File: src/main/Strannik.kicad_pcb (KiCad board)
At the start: 2 copper layers, 139 x 129 mm, 104 parts, among them J1 Thumb cluster, J2 Battery, SW1 Reset, SW11 SW_Push_Dual, SW12 SW_Push_Dual, SW13 SW_Push_Dual, SW14 SW_Push_Dual, SW15 SW_Push_Dual, SW16 SW_Push_Dual, SW17 SW_Push_Dual, SW21 SW_Push_Dual, SW22 SW_Push_Dual, SW23 SW_Push_Dual, SW24 SW_Push_Dual, SW25 SW_Push_Dual, SW26 SW_Push_Dual, SW27 SW_Push_Dual, SW31 SW_Push_Dual, SW32 SW_Push_Dual, SW33 SW_Push_Dual, SW34 SW_Push_Dual, SW35 SW_Push_Dual, SW36 SW_Push_Dual, SW37 SW_Push_Dual, SW41 SW_Push_Dual, SW42 SW_Push_Dual, SW43 SW_Push_Dual, SW44 SW_Push_Dual, SW45 SW_Push_Dual, SW46 SW_Push_Dual, SW51 SW_Push_Dual, SW52 SW_Push_Dual, SW53 SW_Push_Dual, SW54 SW_Push_Dual, SW55 SW_Push_Dual

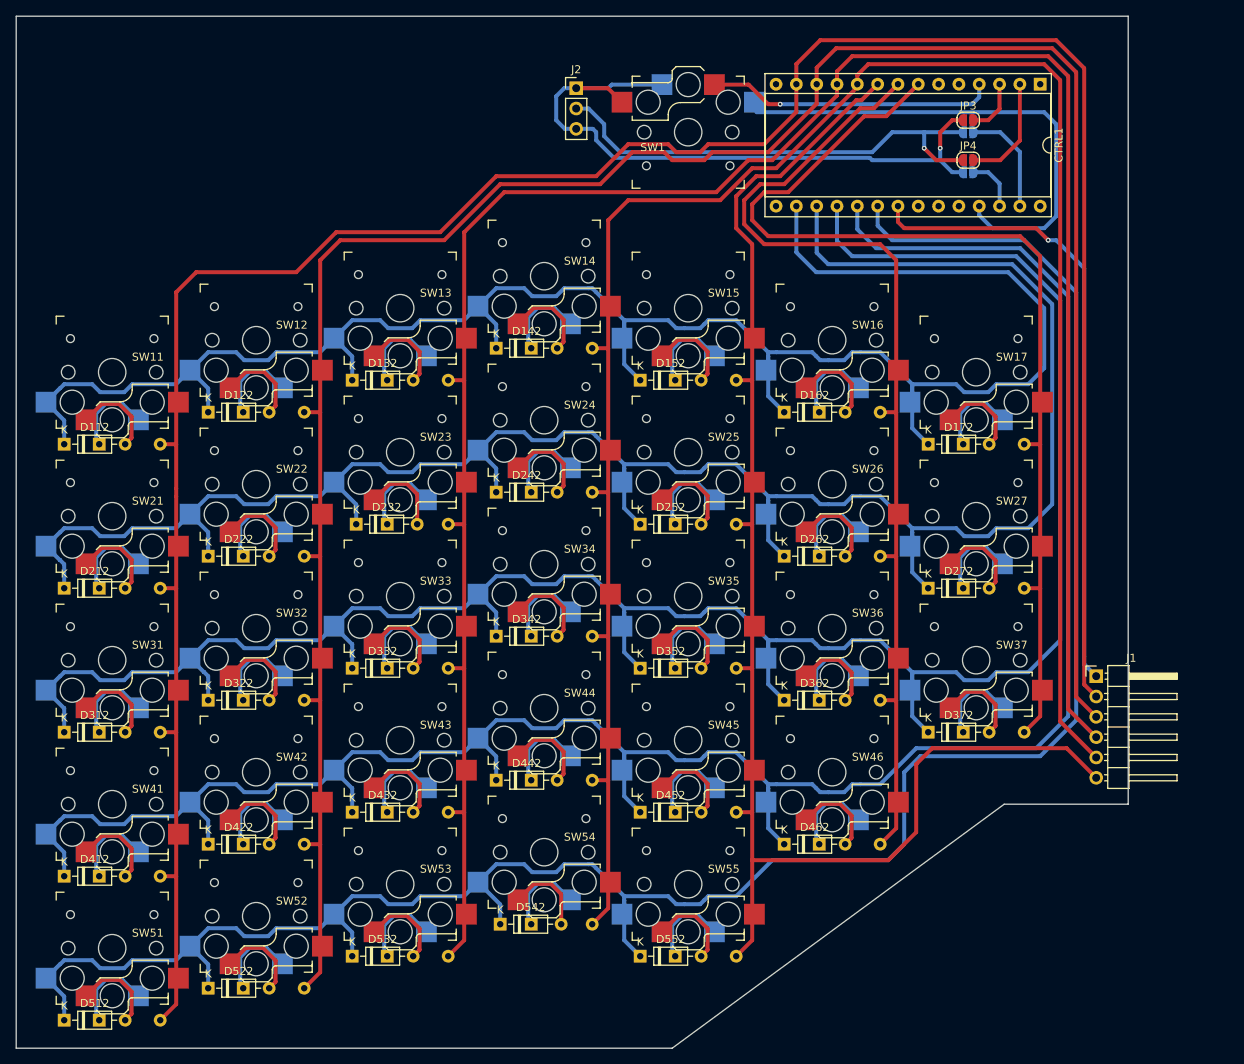
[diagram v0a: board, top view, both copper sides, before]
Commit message: Layout improvements for main pcb
* increased column stagger by 1mm
* tightened switch placement inside column by 1mm, following cap size
* tightened copper on board, making it 5mm smaller vertically
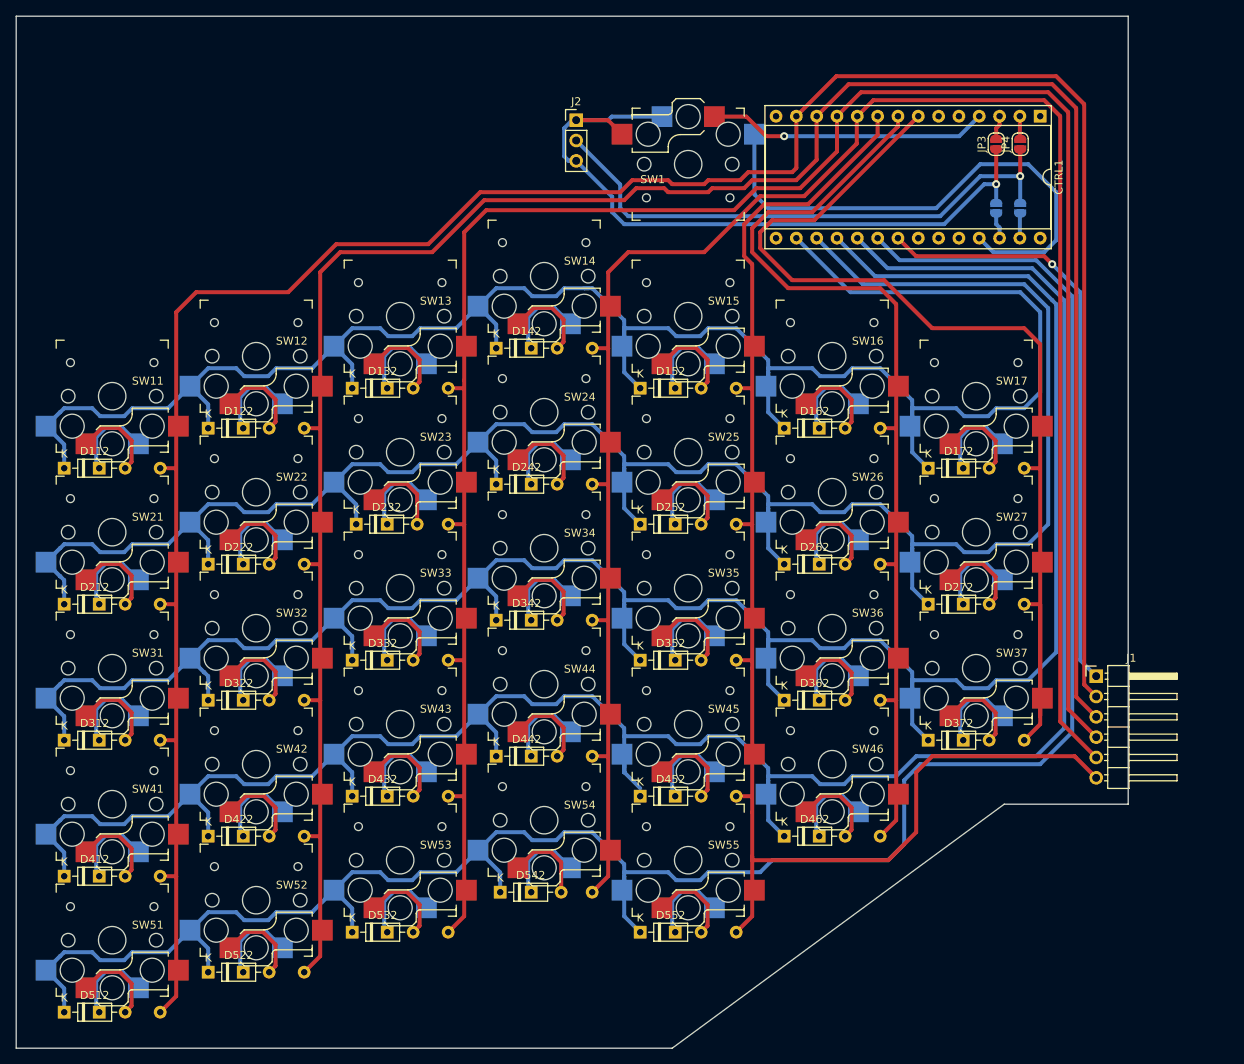
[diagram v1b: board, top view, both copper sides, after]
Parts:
- moved JP2 11.5 mm to (170.5, 59.0), turned to -90 degrees
- moved JP4 6.80 mm to (170.5, 51.0), turned to 90 degrees
- moved JP1 5.70 mm to (167.5, 59.0), turned to -90 degrees
- moved JP3 4.61 mm to (167.5, 51.0), turned to 90 degrees
- moved CTRL1 4.00 mm to (173.0, 47.5)
- moved D541 4.00 mm to (109.4, 144.5)
- moved D542 4.00 mm to (105.5, 144.5)
- moved J2 4.00 mm to (115.0, 48.0)
- moved SW1 4.00 mm to (129.0, 53.5)
- moved SW54 4.00 mm to (111.0, 135.5)
- moved D111 3.00 mm to (55.4, 91.5)
- moved D112 3.00 mm to (51.0, 91.5)
- moved D171 3.00 mm to (163.4, 91.5)
- moved D172 3.00 mm to (159.0, 91.5)
- moved D441 3.00 mm to (109.4, 127.5)
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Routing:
- net Net-(CTRL1-Pin_10): track 249.6 -> 236.6 mm
- net Net-(CTRL1-Pin_2): track 13.9 -> 2.87 mm
- net Net-(CTRL1-Pin_27): track 13.6 -> 3.11 mm
- net Net-(J2-Pin_2): track 60.0 -> 69.9 mm
- net Net-(CTRL1-Pin_12): track 291.6 -> 282.5 mm
- net Net-(CTRL1-Pin_13): track 311.3 -> 302.4 mm
- net Net-(CTRL1-Pin_11): track 270.8 -> 262.3 mm
- net Net-(CTRL1-Pin_9): track 183.4 -> 175.8 mm
- net Net-(CTRL1-Pin_8): track 128.9 -> 121.8 mm
- net Net-(J2-Pin_1): track 84.4 -> 90.3 mm
- net Net-(CTRL1-Pin_25): track 61.6 -> 66.7 mm
- net Net-(CTRL1-Pin_7): track 131.2 -> 136.1 mm
- net Net-(CTRL1-Pin_21): track 79.3 -> 74.4 mm
- net Net-(CTRL1-Pin_3): track 6.94 -> 3.02 mm
- net Net-(CTRL1-Pin_26): track 6.68 -> 3.26 mm
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
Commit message: new beautiful main board design
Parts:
- added JP1: Ground Left, Jumper:SolderJumper-2_P1.3mm_Open_RoundedPad1.0x1.5mm, B.Cu at (189.5, 76.5)
- added JP3: Ground Right, Jumper:SolderJumper-2_P1.3mm_Open_RoundedPad1.0x1.5mm, F.Cu at (181.5, 76.5)
- SW1: footprint Keyswitches:Kailh_socket_PG1350_reversible -> Button_Switch_THT:SW_PUSH_6mm_H4.3mm
- moved J2 93.9 mm to (176.5, 119.0), turned to -90 degrees
- moved SW1 77.9 mm to (186.5, 106.0), turned to 0 degrees
- moved JP3 26.9 mm to (181.5, 74.0), turned to 180 degrees
- moved JP1 26.6 mm to (189.5, 74.0), turned to 0 degrees
- moved JP4 23.3 mm to (181.5, 71.5), turned to 180 degrees
- moved JP2 22.7 mm to (189.5, 71.5), turned to 0 degrees
- moved CTRL1 22.1 mm to (178.0, 69.0), turned to 0 degrees
- moved J1 13.2 mm to (193.0, 115.0), turned to -90 degrees
- moved D111 10.5 mm to (54.4, 81.0)
- moved D112 10.5 mm to (50.0, 81.0)
- moved D121 10.5 mm to (72.4, 76.0)
- moved D122 10.5 mm to (68.0, 76.0)
- moved D131 10.5 mm to (90.4, 71.0)
- moved D132 10.5 mm to (86.0, 71.0)
- moved D141 10.5 mm to (108.4, 66.0)
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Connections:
- D112 pad 1: Net-(CTRL1-Pin_16) -> Net-(CTRL1-Pin_21)
- D122 pad 1: Net-(CTRL1-Pin_16) -> Net-(CTRL1-Pin_21)
- D132 pad 1: Net-(CTRL1-Pin_16) -> Net-(CTRL1-Pin_21)
- D142 pad 1: Net-(CTRL1-Pin_16) -> Net-(CTRL1-Pin_21)
- D152 pad 1: Net-(CTRL1-Pin_16) -> Net-(CTRL1-Pin_21)
- D162 pad 1: Net-(CTRL1-Pin_16) -> Net-(CTRL1-Pin_21)
- D172 pad 1: Net-(CTRL1-Pin_16) -> Net-(CTRL1-Pin_21)
- D212 pad 1: Net-(CTRL1-Pin_17) -> Net-(CTRL1-Pin_20)
- D222 pad 1: Net-(CTRL1-Pin_17) -> Net-(CTRL1-Pin_20)
- D232 pad 1: Net-(CTRL1-Pin_17) -> Net-(CTRL1-Pin_20)
- D242 pad 1: Net-(CTRL1-Pin_17) -> Net-(CTRL1-Pin_20)
- D252 pad 1: Net-(CTRL1-Pin_17) -> Net-(CTRL1-Pin_20)
- D262 pad 1: Net-(CTRL1-Pin_17) -> Net-(CTRL1-Pin_20)
- D272 pad 1: Net-(CTRL1-Pin_17) -> Net-(CTRL1-Pin_20)
- D312 pad 1: Net-(CTRL1-Pin_18) -> Net-(CTRL1-Pin_19)
- D322 pad 1: Net-(CTRL1-Pin_18) -> Net-(CTRL1-Pin_19)
- D332 pad 1: Net-(CTRL1-Pin_18) -> Net-(CTRL1-Pin_19)
- D342 pad 1: Net-(CTRL1-Pin_18) -> Net-(CTRL1-Pin_19)
- D352 pad 1: Net-(CTRL1-Pin_18) -> Net-(CTRL1-Pin_19)
- D362 pad 1: Net-(CTRL1-Pin_18) -> Net-(CTRL1-Pin_19)
- D372 pad 1: Net-(CTRL1-Pin_18) -> Net-(CTRL1-Pin_19)
- D412 pad 1: Net-(CTRL1-Pin_19) -> Net-(CTRL1-Pin_18)
- D422 pad 1: Net-(CTRL1-Pin_19) -> Net-(CTRL1-Pin_18)
- D432 pad 1: Net-(CTRL1-Pin_19) -> Net-(CTRL1-Pin_18)
- D442 pad 1: Net-(CTRL1-Pin_19) -> Net-(CTRL1-Pin_18)
- D452 pad 1: Net-(CTRL1-Pin_19) -> Net-(CTRL1-Pin_18)
- D462 pad 1: Net-(CTRL1-Pin_19) -> Net-(CTRL1-Pin_18)
- D512 pad 1: Net-(CTRL1-Pin_20) -> Net-(CTRL1-Pin_17)
- D522 pad 1: Net-(CTRL1-Pin_20) -> Net-(CTRL1-Pin_17)
- D532 pad 1: Net-(CTRL1-Pin_20) -> Net-(CTRL1-Pin_17)
- D542 pad 1: Net-(CTRL1-Pin_20) -> Net-(CTRL1-Pin_17)
- D552 pad 1: Net-(CTRL1-Pin_20) -> Net-(CTRL1-Pin_17)
- J1 pad 1: Net-(CTRL1-Pin_21) -> Net-(CTRL1-Pin_16)
- J1 pad 2: Net-(CTRL1-Pin_13) -> Net-(CTRL1-Pin_9)
- J1 pad 3: Net-(CTRL1-Pin_12) -> Net-(CTRL1-Pin_10)
- J1 pad 5: Net-(CTRL1-Pin_10) -> Net-(CTRL1-Pin_12)
- J1 pad 6: Net-(CTRL1-Pin_9) -> Net-(CTRL1-Pin_13)
- SW11 pad 2: Net-(CTRL1-Pin_16) -> Net-(CTRL1-Pin_21)
- SW12 pad 2: Net-(CTRL1-Pin_16) -> Net-(CTRL1-Pin_21)
- SW13 pad 2: Net-(CTRL1-Pin_16) -> Net-(CTRL1-Pin_21)
- SW14 pad 2: Net-(CTRL1-Pin_16) -> Net-(CTRL1-Pin_21)
- SW15 pad 2: Net-(CTRL1-Pin_16) -> Net-(CTRL1-Pin_21)
- SW16 pad 2: Net-(CTRL1-Pin_16) -> Net-(CTRL1-Pin_21)
- SW17 pad 2: Net-(CTRL1-Pin_16) -> Net-(CTRL1-Pin_21)
- SW21 pad 2: Net-(CTRL1-Pin_17) -> Net-(CTRL1-Pin_20)
- SW22 pad 2: Net-(CTRL1-Pin_17) -> Net-(CTRL1-Pin_20)
- SW23 pad 2: Net-(CTRL1-Pin_17) -> Net-(CTRL1-Pin_20)
- SW24 pad 2: Net-(CTRL1-Pin_17) -> Net-(CTRL1-Pin_20)
- SW25 pad 2: Net-(CTRL1-Pin_17) -> Net-(CTRL1-Pin_20)
- SW26 pad 2: Net-(CTRL1-Pin_17) -> Net-(CTRL1-Pin_20)
- SW27 pad 2: Net-(CTRL1-Pin_17) -> Net-(CTRL1-Pin_20)
- SW31 pad 2: Net-(CTRL1-Pin_18) -> Net-(CTRL1-Pin_19)
- SW32 pad 2: Net-(CTRL1-Pin_18) -> Net-(CTRL1-Pin_19)
- SW33 pad 2: Net-(CTRL1-Pin_18) -> Net-(CTRL1-Pin_19)
- SW34 pad 2: Net-(CTRL1-Pin_18) -> Net-(CTRL1-Pin_19)
- SW35 pad 2: Net-(CTRL1-Pin_18) -> Net-(CTRL1-Pin_19)
- SW36 pad 2: Net-(CTRL1-Pin_18) -> Net-(CTRL1-Pin_19)
- SW37 pad 2: Net-(CTRL1-Pin_18) -> Net-(CTRL1-Pin_19)
- SW41 pad 2: Net-(CTRL1-Pin_19) -> Net-(CTRL1-Pin_18)
- SW42 pad 2: Net-(CTRL1-Pin_19) -> Net-(CTRL1-Pin_18)
- SW43 pad 2: Net-(CTRL1-Pin_19) -> Net-(CTRL1-Pin_18)
- SW44 pad 2: Net-(CTRL1-Pin_19) -> Net-(CTRL1-Pin_18)
- SW45 pad 2: Net-(CTRL1-Pin_19) -> Net-(CTRL1-Pin_18)
- SW46 pad 2: Net-(CTRL1-Pin_19) -> Net-(CTRL1-Pin_18)
- SW51 pad 2: Net-(CTRL1-Pin_20) -> Net-(CTRL1-Pin_17)
- SW52 pad 2: Net-(CTRL1-Pin_20) -> Net-(CTRL1-Pin_17)
- SW53 pad 2: Net-(CTRL1-Pin_20) -> Net-(CTRL1-Pin_17)
- SW54 pad 2: Net-(CTRL1-Pin_20) -> Net-(CTRL1-Pin_17)
- SW55 pad 2: Net-(CTRL1-Pin_20) -> Net-(CTRL1-Pin_17)
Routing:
- net Net-(CTRL1-Pin_16): track 247.3 -> 17.1 mm
- net Net-(CTRL1-Pin_21): track 74.4 -> 259.9 mm, vias 1 -> 0
- net Net-(CTRL1-Pin_7): track 136.1 -> 64.3 mm
- net Net-(CTRL1-Pin_18): track 279.4 -> 227.9 mm
- net Net-(CTRL1-Pin_19): track 279.6 -> 230.8 mm
- net Net-(CTRL1-Pin_17): track 262.4 -> 217.5 mm
- net Net-(CTRL1-Pin_13): track 302.4 -> 260.8 mm, vias 0 -> 1
- net Net-(CTRL1-Pin_12): track 282.5 -> 243.8 mm, vias 0 -> 1
- net Net-(CTRL1-Pin_10): track 236.6 -> 198.7 mm, vias 0 -> 1
- net Net-(CTRL1-Pin_11): track 262.3 -> 225.3 mm, vias 0 -> 1
- net Net-(CTRL1-Pin_4): track 35.2 -> 2.90 mm, vias 1 -> 0
- net Net-(CTRL1-Pin_20): track 271.2 -> 241.9 mm
- net Net-(CTRL1-Pin_25): track 66.7 -> 44.7 mm, vias 0 -> 1
- net Net-(J2-Pin_1): track 90.3 -> 69.5 mm
- net Net-(CTRL1-Pin_9): track 175.8 -> 189.4 mm
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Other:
- board size 139 x 129 mm -> 150 x 106.5 mm
